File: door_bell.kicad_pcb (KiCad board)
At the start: 4 copper layers, 68.6 x 68.6 mm, 75 parts, among them J1 8-10V AC/DC, J2 Speaker, J3 SWITCH1, J5 UART, J6 JTAG, J7 BOOT, J8 MicroSD, J9 Door panel, K1 HJR 1-2C, Q1 BC338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

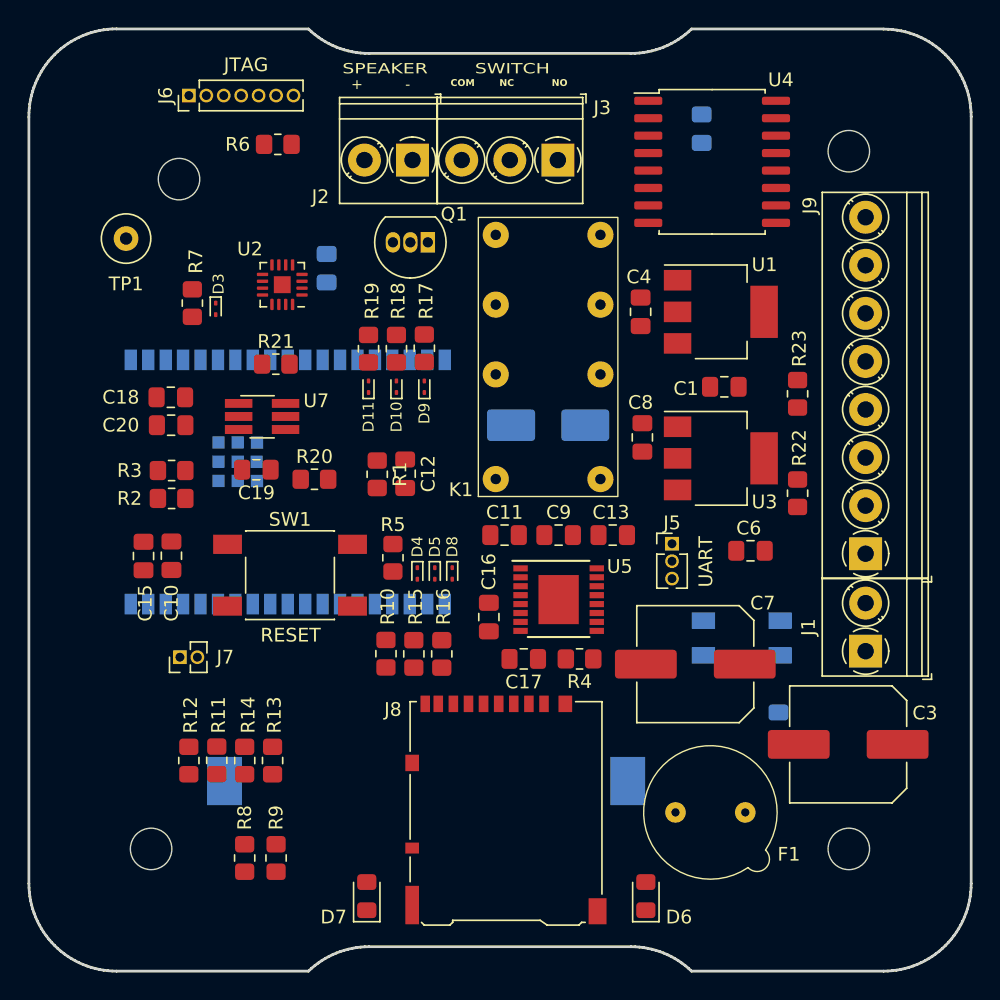
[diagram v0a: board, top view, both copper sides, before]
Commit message: Part placement and silk screen adjustments
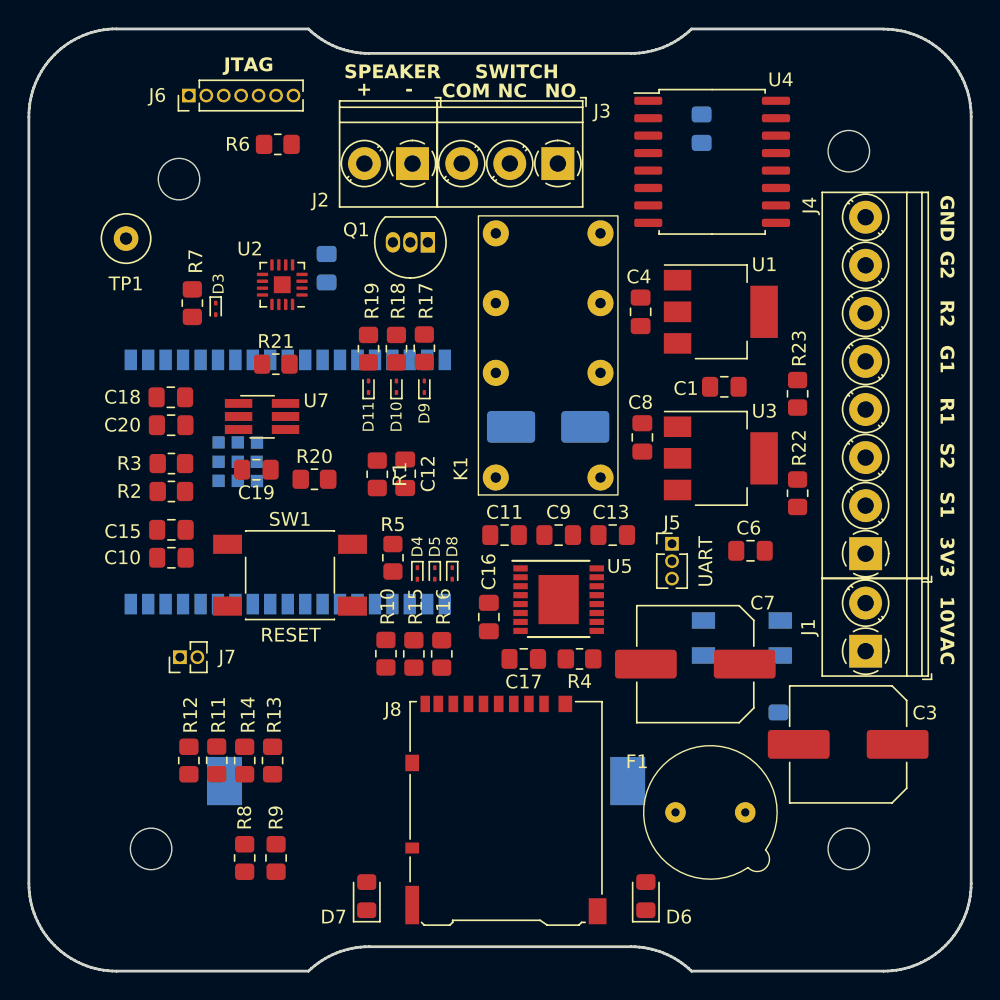
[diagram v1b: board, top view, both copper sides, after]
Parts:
- moved C15 2.79 mm to (115.3, 90.2), turned to 180 degrees
- moved R3 0.51 mm to (115.3, 85.3)
- moved R2 0.51 mm to (115.3, 87.4)
- moved J2 0.25 mm to (132.9, 63.5)
- moved J3 0.25 mm to (143.5, 63.5)
- moved C10 0.15 mm to (115.3, 92.2), turned to 180 degrees
- moved D2 0.13 mm to (142.7, 82.7)
- moved K1 0.11 mm to (146.6, 86.4)
- renumbered J9 to J4
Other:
- board text added: "10VAC"
- board text added: "3V3"
- board text added: "G1"
- board text added: "G2"
- board text added: "GND"
- board text added: "R1"
- board text added: "R2"
- board text added: "S1"
- board text added: "S2"

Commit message: Silk screen adjustments
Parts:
- moved Q1 3.48 mm to (130.6, 69.8), turned to 0 degrees
- moved C12 0.93 mm to (133.1, 86.6)
- moved R17 0.64 mm to (134.4, 77.0)
- moved R19 0.64 mm to (129.0, 77.0)
- moved D9 0.64 mm to (134.4, 79.7)
- moved D11 0.63 mm to (129.0, 79.7)
- moved R1 0.53 mm to (130.3, 86.7)
- moved SW1 0.34 mm to (123.7, 93.2), turned to 0 degrees

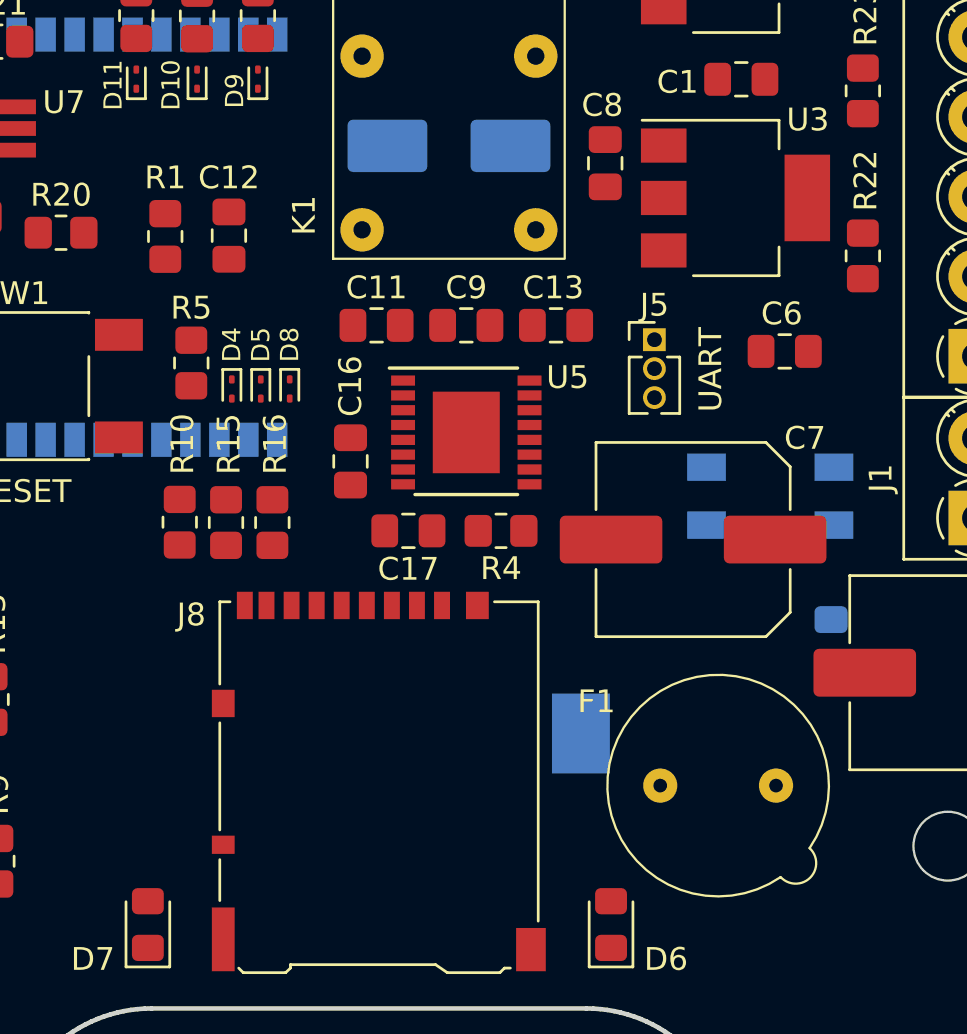
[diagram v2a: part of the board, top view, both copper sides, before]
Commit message: Adapting after placing 3D model of fuse F1
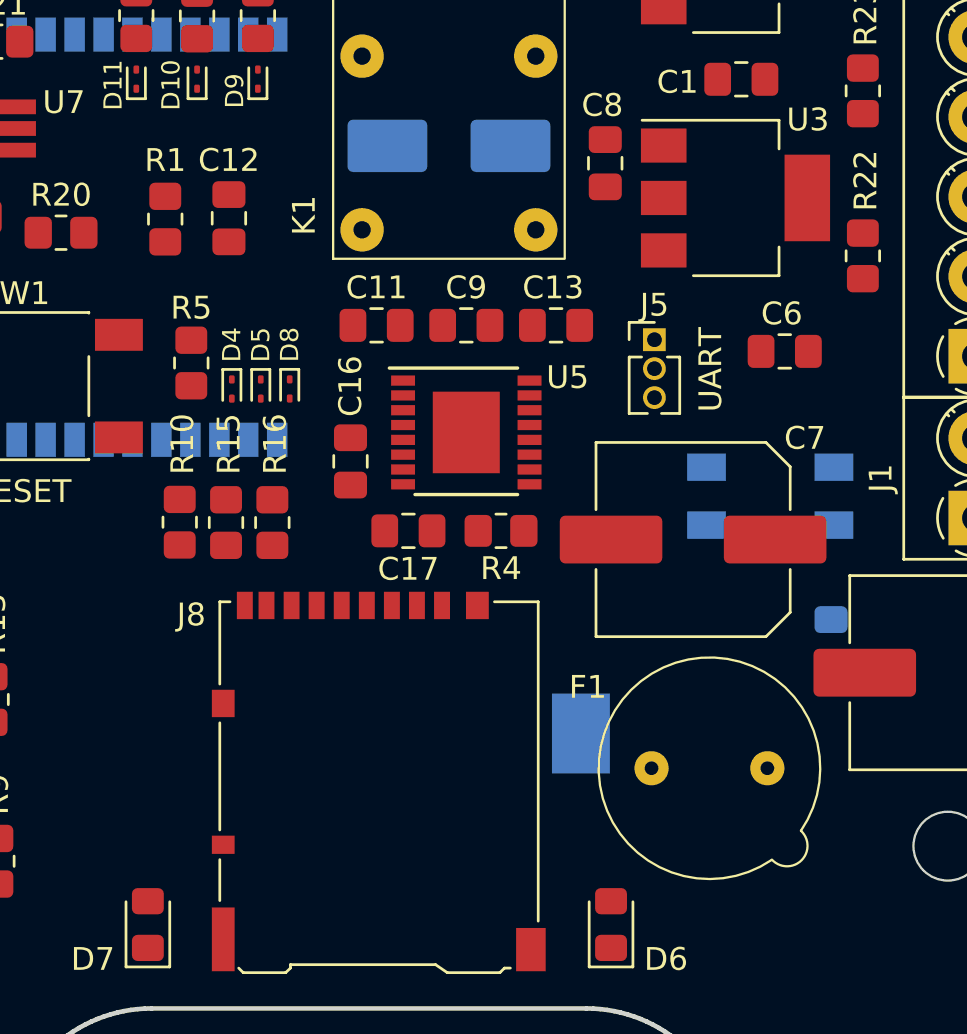
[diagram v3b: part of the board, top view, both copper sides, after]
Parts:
- moved F1 0.85 mm to (151.6, 110.0)
- moved C12 0.76 mm to (133.1, 85.9)
- moved R1 0.76 mm to (130.3, 85.9)
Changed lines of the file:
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@@
     )
   )
+  (footprint "Fuse_espena:FuseHolder_Keystone_3554" (layer "F.Cu")
+    (at 151.638 109.982)
+    (property "Sheetfile" "door_bell.kicad_sch")
+    (property "Sheetname" "")
+    (property "ki_description" "Fuse")
+    (property "ki_keywords" "fuse")
+    (attr through_hole)
+    (fp_text reference "F1" (at -2.794 -3.556 unlocked) (layer "F.SilkS")
+        (effects (font (size 1 1) (thickness 0.1)))
+    )
+    (fp_text value "1A" (at 3.302 9.398 unlocked) (layer "F.Fab") hide
+        (effects (font (size 1 1) (thickness 0.15)))
+    )
+    (fp_arc (start 5.26581 4.025031) (mid -0.889918 -3.44479) (end 6.5532 2.7432)
+      (stroke (width 0.1) (type default)) (layer "F.SilkS"))
+    (fp_arc (start 6.553199 2.743201) (mid 6.578034 4.040178) (end 5.281148 4.010968)
+      (stroke (width 0.1) (type default)) (layer "F.SilkS"))
+    (fp_circle (center 0 0) (end 0.508 0.762)
+      (stroke (width 0.05) (type default)) (fill none) (layer "B.CrtYd"))
+    (fp_circle (center 5.05319 0) (end 5.56119 0.762)
+      (stroke (width 0.05) (type default)) (fill none) (layer "B.CrtYd"))
+    (fp_arc (start 5.334 4.318) (mid -1.096727 -3.636727) (end 6.858 2.794)
+      (stroke (width 0.05) (type default)) (layer "F.CrtYd"))
+    (fp_arc (start 6.858 2.794) (mid 6.720947 4.172878) (end 5.34173 4.306481)
+      (stroke (width 0.05) (type default)) (layer "F.CrtYd"))
+    (pad "1" thru_hole circle (at 0 0) (size 1.5 1.5) (drill 0.6) (layers "*.Cu" "*.Mask")
+      (net 17 "Net-(D1-Pad4)") (pintype "passive"))
+    (pad "2" thru_hole circle (at 5.08 0) (size 1.5 1.5) (drill 0.6) (layers "*.Cu" "*.Mask")
+      (net 28 "Net-(J1-Pin_2)") (pintype "passive"))
+    (model ":KICAD7_3RD_PARTY:3dmodels/Fuse_espena.3dshapes/Fuse_MXT250_With_Socket.step" hide
+      (offset (xyz 0 0 0))
+      (scale (xyz 1 1 1))
+      (rotate (xyz 0 0 0))
+    )
+    (model ":KICAD7_3RD_PARTY:3dmodels/Fuse_espena.3dshapes/Fuse_MXT250.step"
+      (offset (xyz 0 0 0))
+      (scale (xyz 1 1 1))
+      (rotate (xyz 0 0 0))
+    )
+  )
   (footprint "Diode_SMD:D_SOD-923" (layer "F.Cu")
     (at 131.699 79.749 90)
@@
     )
   )
-  (footprint "Fuse_espena:FuseHolder_Keystone_3554" (layer "F.Cu")
-    (at 152.019 110.744)
-    (property "Sheetfile" "door_bell.kicad_sch")
-    (property "Sheetname" "")
-    (property "ki_description" "Fuse")
-    (property "ki_keywords" "fuse")
-    (attr through_hole)
-    (fp_text reference "F1" (at -2.794 -3.683 unlocked) (layer "F.SilkS")
-        (effects (font (size 1 1) (thickness 0.1)))
-    )
-    (fp_text value "1A" (at 3.302 9.398 unlocked) (layer "F.Fab") hide
-        (effects (font (size 1 1) (thickness 0.15)))
-    )
-    (fp_arc (start 5.26581 4.025031) (mid -0.889918 -3.44479) (end 6.5532 2.7432)
-      (stroke (width 0.1) (type default)) (layer "F.SilkS"))
-    (fp_arc (start 6.553199 2.743201) (mid 6.578034 4.040178) (end 5.281148 4.010968)
-      (stroke (width 0.1) (type default)) (layer "F.SilkS"))
-    (fp_circle (center 0 0) (end 0.508 0.762)
-      (stroke (width 0.05) (type default)) (fill none) (layer "B.CrtYd"))
-    (fp_circle (center 5.05319 0) (end 5.56119 0.762)
-      (stroke (width 0.05) (type default)) (fill none) (layer "B.CrtYd"))
-    (fp_arc (start 5.334 4.318) (mid -1.096727 -3.636727) (end 6.858 2.794)
-      (stroke (width 0.05) (type default)) (layer "F.CrtYd"))
-    (fp_arc (start 6.858 2.794) (mid 6.720947 4.172878) (end 5.34173 4.306481)
-      (stroke (width 0.05) (type default)) (layer "F.CrtYd"))
-    (pad "1" thru_hole circle (at 0 0) (size 1.5 1.5) (drill 0.6) (layers "*.Cu" "*.Mask")
-      (net 17 "Net-(D1-Pad4)") (pintype "passive"))
-    (pad "2" thru_hole circle (at 5.08 0) (size 1.5 1.5) (drill 0.6) (layers "*.Cu" "*.Mask")
-      (net 28 "Net-(J1-Pin_2)") (pintype "passive"))
-  )
   (footprint "Package_SO:SOIC-16W_7.5x10.3mm_P1.27mm" (layer "F.Cu")
     (at 154.686 63.373)
@@
   )
   (footprint "Capacitor_SMD:C_0805_2012Metric_Pad1.18x1.45mm_HandSolder" (layer "F.Cu")
-    (at 133.096 86.614 -90)
+    (at 133.096 85.852 -90)
     (descr "Capacitor SMD 0805 (2012 Metric), square (rectangular) end terminal, IPC_7351 nominal with elongated pad for handsoldering. (Body size source: IPC-SM-782 page 76, https://www.pcb-3d.com/wordpress/wp-content/uploads/ipc-sm-782a_amendment_1_and_2.pdf, https://docs.google.com/spreadsheets/d/1BsfQQcO9C6DZCsRaXUlFlo91Tg2WpOkGARC1WS5S8t0/edit?usp=sharing), generated with kicad-footprint-generator")
     (tags "capacitor handsolder")
@@
   )
   (footprint "Resistor_SMD:R_0805_2012Metric_Pad1.20x1.40mm_HandSolder" (layer "F.Cu")
-    (at 130.302 86.6515 -90)
+    (at 130.302 85.8895 -90)
     (descr "Resistor SMD 0805 (2012 Metric), square (rectangular) end terminal, IPC_7351 nominal with elongated pad for handsoldering. (Body size source: IPC-SM-782 page 72, https://www.pcb-3d.com/wordpress/wp-content/uploads/ipc-sm-782a_amendment_1_and_2.pdf), generated with kicad-footprint-generator")
     (tags "resistor handsolder")

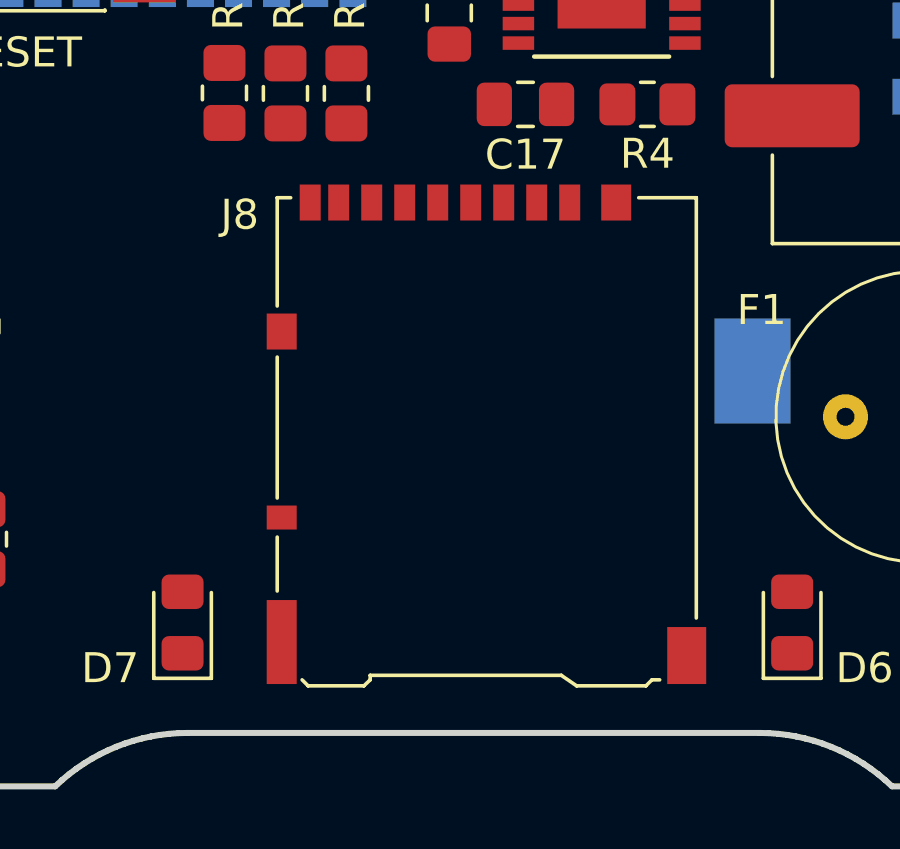
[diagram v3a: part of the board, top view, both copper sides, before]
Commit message: Setting up footprints and 3D models
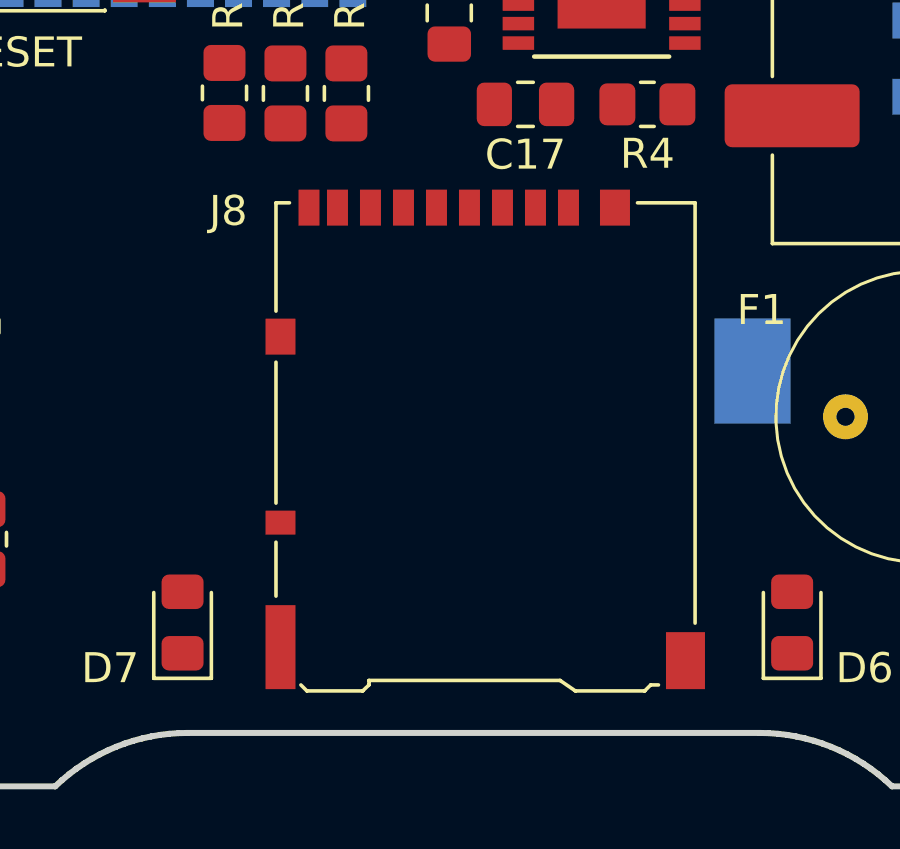
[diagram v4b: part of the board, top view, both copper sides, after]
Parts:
- moved J8 0.17 mm to (139.6, 110.7)
